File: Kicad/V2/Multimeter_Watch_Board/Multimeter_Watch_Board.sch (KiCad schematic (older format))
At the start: 50 parts, among them J1 S3B-PH-K-S(LF)(SN), J2 S3B-PH-K-S(LF)(SN), J3 S3B-PH-K-S(LF)(SN), J6 51281-1294, J7 Conn_01x11_Female, J8 Conn_01x11_Female, Q1 A03400A N-MOS, U1 PCF85163-SO08, U2 AD8592, Y1 32kHz

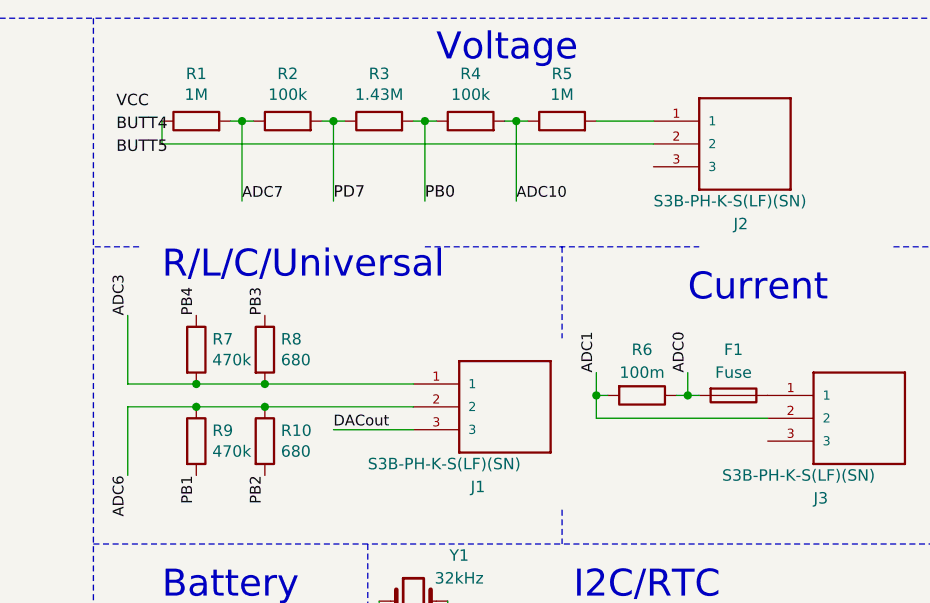
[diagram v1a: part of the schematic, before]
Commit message: change voltage/current connector setup from pins 1-2 to 1-3 for greater distance between voltage input pins
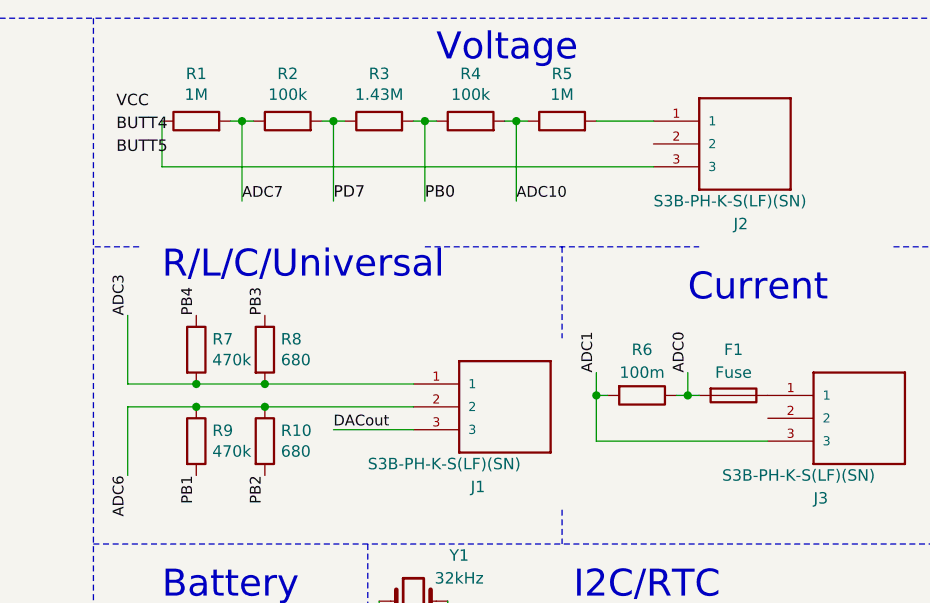
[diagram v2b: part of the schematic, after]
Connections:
- net ADC1: now also J3.3; no longer J3.2
- net at R1.1: now also J2.3; no longer J2.2
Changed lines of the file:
@@
 Wire Wire Line
 	6700 950  6750 950
-Wire Wire Line
-	5200 950  5200 1050
 $Comp
 L Device:R R2
@@
 Text Notes 5200 1650 0    118  ~ 0
 R/L/C/Universal\n
-Wire Wire Line
-	7100 2150 7100 2250
-Wire Wire Line
-	6300 2300 5950 2300
-Text Label 5950 2300 0    47   ~ 0
-DACout
-$Comp
-L Device:R R9
-U 1 1 5F1F5ED9
-P 5350 2350
-F 0 "R9" H 5420 2396 50  0000 L CNN
-F 1 "470k" H 5420 2305 50  0000 L CNN
-F 2 "Resistor_SMD:R_0805_2012Metric_Pad1.15x1.40mm_HandSolder" V 5280 2350 50  0001 C CNN
-F 3 "~" H 5350 2350 50  0001 C CNN
-	1    5350 2350
-	1    0    0    -1
-$EndComp
-$Comp
-L Device:R R10
-U 1 1 5F1F5EE3
-P 5650 2350
-F 0 "R10" H 5720 2396 50  0000 L CNN
-F 1 "680" H 5720 2305 50  0000 L CNN
-F 2 "Resistor_SMD:R_0805_2012Metric_Pad1.15x1.40mm_HandSolder" V 5580 2350 50  0001 C CNN
-F 3 "~" H 5650 2350 50  0001 C CNN
-	1    5650 2350
-	1    0    0    -1
-$EndComp
 $Comp
 L Device:R R7
@@
 $EndComp
 Wire Wire Line
-	6300 2200 5650 2200
-Wire Wire Line
-	5650 2200 5350 2200
-Connection ~ 5650 2200
-Wire Wire Line
-	5350 2200 5050 2200
-Wire Wire Line
-	5050 2200 5050 2500
-Connection ~ 5350 2200
-Wire Wire Line
 	6300 2100 5650 2100
 Wire Wire Line
@@
 	5050 2100 5050 1800
 Connection ~ 5350 2100
-Text Label 5350 2500 3    47   ~ 0
-PB1
-Text Label 5650 2500 3    47   ~ 0
-PB2
 Text Label 5650 1800 1    47   ~ 0
 PB3
@@
 Text Label 5550 1300 0    47   ~ 0
 ADC7
-Text Label 5050 2500 3    47   ~ 0
-ADC6
 Wire Notes Line
 	6350 1500 7550 1500
@@
 Wire Wire Line
 	7500 2150 7450 2150
-Wire Wire Line
-	7100 2250 7850 2250
 Text Label 6350 1300 0    50   ~ 0
 PB0
-Wire Wire Line
-	5200 1050 7350 1050
 Wire Wire Line
 	7350 950  7100 950
@@
 Text Label 7750 5650 2    50   ~ 0
 PE4
+Text Label 5050 2500 3    47   ~ 0
+ADC6
+Text Label 5650 2500 3    47   ~ 0
+PB2
+Text Label 5350 2500 3    47   ~ 0
+PB1
+Connection ~ 5350 2200
+Wire Wire Line
+	5050 2200 5050 2500
+Wire Wire Line
+	5350 2200 5050 2200
+Connection ~ 5650 2200
+Wire Wire Line
+	5650 2200 5350 2200
+Wire Wire Line
+	6300 2200 5650 2200
+$Comp
+L Device:R R10
+U 1 1 5F1F5EE3
+P 5650 2350
+F 0 "R10" H 5720 2396 50  0000 L CNN
+F 1 "680" H 5720 2305 50  0000 L CNN
+F 2 "Resistor_SMD:R_0805_2012Metric_Pad1.15x1.40mm_HandSolder" V 5580 2350 50  0001 C CNN
+F 3 "~" H 5650 2350 50  0001 C CNN
+	1    5650 2350
+	1    0    0    -1
+$EndComp
+$Comp
+L Device:R R9
+U 1 1 5F1F5ED9
+P 5350 2350
+F 0 "R9" H 5420 2396 50  0000 L CNN
+F 1 "470k" H 5420 2305 50  0000 L CNN
+F 2 "Resistor_SMD:R_0805_2012Metric_Pad1.15x1.40mm_HandSolder" V 5280 2350 50  0001 C CNN
+F 3 "~" H 5350 2350 50  0001 C CNN
+	1    5350 2350
+	1    0    0    -1
+$EndComp
+Wire Wire Line
+	6300 2300 5950 2300
+Text Label 5950 2300 0    47   ~ 0
+DACout
+Wire Wire Line
+	7100 2350 7850 2350
+Wire Wire Line
+	7100 2150 7100 2350
+Wire Wire Line
+	5200 1150 7350 1150
+Wire Wire Line
+	5200 950  5200 1150
 $EndSCHEMATC
